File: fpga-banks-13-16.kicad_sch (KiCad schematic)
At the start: 48 parts, among them U14 XC7A100T-FGG484, U15 Oscillator_100MHz_AMJMEFB

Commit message: pcb final
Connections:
- net ROT_GPIO1: now also U14.N14 (IO_L23N_T3_A02_D18_14); no longer U14.M16 (IO_L24N_T3_RS0_15)
- net ROT_GPIO2: now also U14.U20 (IO_L11P_T1_SRCC_14); no longer U14.F21 (IO_25_16)
- net ROT_MISO: now also U14.K13 (IO_L19P_T3_A22_15); no longer U14.R19 (IO_L5N_T0_D07_14)
- net ROT_MOSI: now also U14.W20 (IO_L12N_T1_MRCC_14); no longer U14.L16 (IO_L23P_T3_FOE_B_15)
- net ROT_RDY\ROT_GPIO0: now also U14.F21 (IO_25_16); no longer U14.F20 (IO_L18N_T2_16)
- net ROT_RX: now also U14.G22 (IO_L24N_T3_16); no longer U14.N14 (IO_L23N_T3_A02_D18_14)
- net ROT_SCLK: now also U14.M16 (IO_L24N_T3_RS0_15); no longer U14.M13 (IO_L20P_T3_A20_15)
- net ROT_SS: now also U14.M13 (IO_L20P_T3_A20_15); no longer U14.U20 (IO_L11P_T1_SRCC_14)
- net ROT_TX: now also U14.F20 (IO_L18N_T2_16); no longer U14.G22 (IO_L24N_T3_16)
- net TPM_PIRQ#: now also U14.L16 (IO_L23P_T3_FOE_B_15); no longer U14.K13 (IO_L19P_T3_A22_15)
- net TPM_RST: now also U14.R19 (IO_L5N_T0_D07_14); no longer U14.W20 (IO_L12N_T1_MRCC_14)

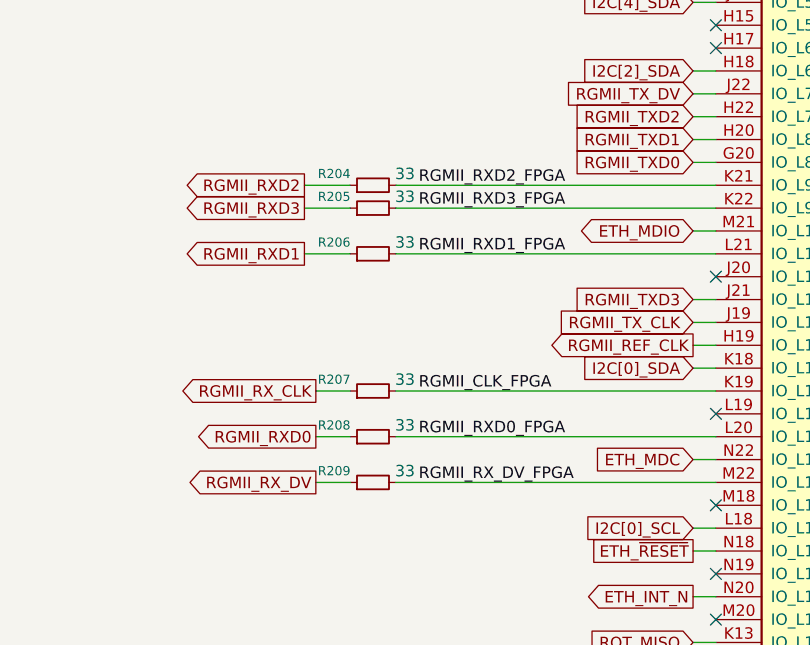
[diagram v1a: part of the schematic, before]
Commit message: bom changes
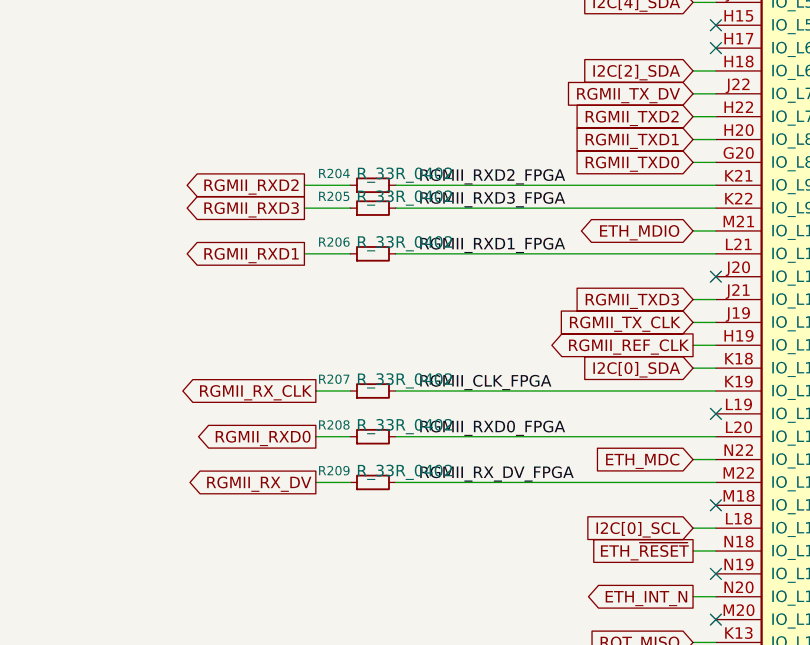
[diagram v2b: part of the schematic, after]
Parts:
- R161: MPN ERJ2GE0R00X -> RC0402JR-7D0RL; Manufacturer Panasonic -> YAGEO
- R204, R205, R206, R207, R208, R209: value 33 -> R_33R_0402

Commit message: version 1.0 complete
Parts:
- C92, C93, C94, C95: MPN C1210C476K8RACTU -> C1210C476K8RAC7210
- R133: MPN CR0402-FX-2201GLF -> AC0402FR-7D2K2L; Manufacturer Bourns -> YAGEO
- R134, R135: MPN CR0402-FX-4701GLF -> RC0402FR-7D4K7L; Manufacturer Bourns -> YAGEO
- R204, R205, R206, R207, R208, R209: MPN (none) -> MCS04020C3309FE000; Manufacturer (none) -> Vishay / Beyschlag
- U14: MPN XC7A100T-FGG484 -> XC7A100T-2FGG484C
- U15: MPN AMJMEFB-100.0000T -> ASEMB-100.000MHZ-XY-T

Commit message: "In the process of upgrading the ddr memory"
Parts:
- removed R133: R_2k2_0402, antmicro-footprints:R_0402_1005Metric, symbol antmicroResistors0402:R_2k2_0402
- removed R134, R135: R_4k7_0402, antmicro-footprints:R_0402_1005Metric, symbol antmicroResistors0402:R_4k7_0402
- removed R161: R_0R_0402, antmicro-footprints:R_0402_1005Metric, symbol antmicroResistors0402:R_0R_0402
- added R24, R25, R26, R28, R29: R_4k7_0402, Resistor_SMD:R_0402_1005Metric, symbol antmicroResistors0402:R_4k7_0402
- C92, C93, C94, C95: footprint antmicro-footprints:C_1210_3225Metric -> Capacitor_SMD:C_1210_3225Metric
- R1: footprint antmicro-footprints:R_0402_1005Metric -> Resistor_SMD:R_0402_1005Metric; now not fitted; now left out of the parts list
- R2: footprint antmicro-footprints:R_0402_1005Metric -> Resistor_SMD:R_0402_1005Metric
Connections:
- net VCC3V3: now also R24.1, R25.1, R26.1, R28.1, R29.1
- net QSPI_CS_N: now reaches U14.T19 (IO_L6P_T0_FCS_B_14)
- net QSPI_CS_N: now also R29.2
- net ESPI_ALERT_N: no longer names the net of U14.D16 (IO_L5N_T0_16)
- net ESPI_CLK: no longer names the net of U14.D17 (IO_L12P_T1_MRCC_16)
- net ESPI_CS0_N: no longer names the net of U14.E16 (IO_L5P_T0_16)
- net ESPI_CS1_N: no longer names the net of U14.H13 (IO_L1P_T0_AD0P_15)
- net ESPI_IO0: no longer names the net of U14.C14 (IO_L3P_T0_DQS_16)
- net ESPI_IO1: no longer names the net of U14.E13 (IO_L4P_T0_16)
- net ESPI_IO2: no longer names the net of U14.E17 (IO_L2N_T0_16)
- net ESPI_IO3: no longer names the net of U14.F13 (IO_L1P_T0_16)
- net ESPI_RESET_N: no longer names the net of U14.G13 (IO_L1N_T0_AD0N_15)
- net I2C[0]_SCL: no longer names the net of U14.L18 (IO_L16N_T2_A27_15)
- net I2C[0]_SDA: no longer names the net of U14.K18 (IO_L13P_T2_MRCC_15)
- net I2C[12]_SCL: no longer names the net of U14.N13 (IO_L23P_T3_A03_D19_14)
- net I2C[1]_SCL: no longer names the net of U14.K17 (IO_L21P_T3_DQS_15)
- net I2C[1]_SDA: no longer names the net of U14.K16 (IO_L23N_T3_FWE_B_15)
- net I2C[2]_SCL: no longer names the net of U14.G18 (IO_L4N_T0_15)
- net I2C[2]_SDA: no longer names the net of U14.H18 (IO_L6N_T0_VREF_15)
- net I2C[3]_SCL: no longer names the net of U14.J16 (IO_0_15)
- net I2C[3]_SDA: no longer names the net of U14.F18 (IO_L15P_T2_DQS_16)
- net I2C[4]_SCL: no longer names the net of U14.G17 (IO_L4P_T0_15)
- net I2C[4]_SDA: no longer names the net of U14.J15 (IO_L5P_T0_AD9P_15)
- net I2C[6]_SCL: no longer names the net of U14.L15 (IO_L22N_T3_A16_15)
- net I2C[6]_SDA: no longer names the net of U14.L14 (IO_L22P_T3_A17_15)
- net I2C[7]_SCL: no longer names the net of U14.G15 (IO_L2P_T0_AD8P_15)
- net I2C[7]_SDA: no longer names the net of U14.J14 (IO_L3P_T0_DQS_AD1P_15)
- net I2C[8]_SCL: no longer names the net of U14.K14 (IO_L19N_T3_A21_VREF_15)
- net I2C[8]_SDA: no longer names the net of U14.L13 (IO_L20N_T3_A19_15)
- net I2C[9]_SCL: no longer names the net of U14.P16 (IO_L24P_T3_A01_D17_14)
- net I2C[9]_SDA: no longer names the net of U14.V17 (IO_L16P_T2_CSI_B_14)
- net I3C[0]_SCL_3V3: no longer names the net of U14.C22 (IO_L20P_T3_16)
- net I3C[0]_SDA_3V3: no longer names the net of U14.F19 (IO_L18P_T2_16)
- net I3C[1]_SCL_3V3: no longer names the net of U14.B22 (IO_L20N_T3_16)
- net I3C[1]_SDA_3V3: no longer names the net of U14.C20 (IO_L19N_T3_VREF_16)
- net I3C[2]_SCL_3V3: no longer names the net of U14.A21 (IO_L21N_T3_DQS_16)
- net I3C[2]_SDA_3V3: no longer names the net of U14.B20 (IO_L16P_T2_16)
- net I3C[3]_SCL_3V3: no longer names the net of U14.A20 (IO_L16N_T2_16)
- net I3C[3]_SDA_3V3: no longer names the net of U14.A18 (IO_L17P_T2_16)
- net NCSI_CLK: no longer names the net of U14.B17 (IO_L11P_T1_SRCC_16)
- net NCSI_CRS_DV: no longer names the net of U14.A15 (IO_L9P_T1_DQS_16)
- net NCSI_RXD0: no longer names the net of U14.E14 (IO_L4N_T0_16)
- net NCSI_RXD1: no longer names the net of U14.D14 (IO_L6P_T0_16)
- net NCSI_RXER: no longer names the net of U14.A13 (IO_L10P_T1_16)
- net NCSI_TXD0: no longer names the net of U14.A14 (IO_L10N_T1_16)
- net NCSI_TXD1: no longer names the net of U14.C15 (IO_L3N_T0_DQS_16)
- net NCSI_TXEN: no longer names the net of U14.B15 (IO_L7P_T1_16)
- net PRSNT0_N_R: no longer names the net of U14.C13 (IO_L8P_T1_16)
- net ROT_GPIO1: no longer names the net of U14.N14 (IO_L23N_T3_A02_D18_14)
- net ROT_GPIO2: no longer names the net of U14.U20 (IO_L11P_T1_SRCC_14)
- net ROT_MISO: no longer names the net of U14.K13 (IO_L19P_T3_A22_15)
- net ROT_MOSI: no longer names the net of U14.W20 (IO_L12N_T1_MRCC_14)
- net ROT_QSPI_DQ0 renamed QSPI_D0
- net QSPI_D0: now also R24.2
- net ROT_QSPI_DQ1 renamed QSPI_D1
- net QSPI_D1: now also R25.2
- net ROT_QSPI_DQ2 renamed QSPI_D2
- net QSPI_D2: now also R26.2
- net ROT_QSPI_DQ3 renamed QSPI_D3
- net QSPI_D3: now also R28.2
- net ROT_RDY\ROT_GPIO0: no longer names the net of U14.F21 (IO_25_16)
- net ROT_RX: no longer names the net of U14.G22 (IO_L24N_T3_16)
- net ROT_SCLK: no longer names the net of U14.M16 (IO_L24N_T3_RS0_15)
- net ROT_SS: no longer names the net of U14.M13 (IO_L20P_T3_A20_15)
- net ROT_TX: no longer names the net of U14.F20 (IO_L18N_T2_16)
- net SGPIO_INTR_N: no longer names the net of U14.M15 (IO_L24P_T3_RS1_15)
- net SPI0_CLK_R: no longer names the net of U14.D20 (IO_L19P_T3_16)
- net SPI0_CS_N_R: no longer names the net of U14.E22 (IO_L22P_T3_16)
- net SPI0_MISO_R: no longer names the net of U14.D22 (IO_L22N_T3_16)
- net SPI0_MOSI_R: no longer names the net of U14.E21 (IO_L23P_T3_16)
- net TPM_GPIO: no longer names the net of U14.Y21 (IO_L9P_T1_DQS_14)
- net TPM_PIRQ#: no longer names the net of U14.L16 (IO_L23P_T3_FOE_B_15)
- net TPM_PP: no longer names the net of U14.M17 (IO_25_15)
- net TPM_RST: no longer names the net of U14.R19 (IO_L5N_T0_D07_14)
- net UART0_SCM_RX: no longer names the net of U14.D19 (IO_L14N_T2_SRCC_16)
- net UART0_SCM_TX: no longer names the net of U14.A19 (IO_L17N_T2_16)
- net UART1_SCM_RX: no longer names the net of U14.C19 (IO_L13N_T2_MRCC_16)
- net UART1_SCM_TX: no longer names the net of U14.A16 (IO_L9N_T1_DQS_16)
- net ULPI1_CLKOUT: no longer names the net of U14.W19 (IO_L12P_T1_MRCC_14)
- net ULPI1_DATA0: no longer names the net of U14.AB18 (IO_L17N_T2_A13_D29_14)
- net ULPI1_DATA1: no longer names the net of U14.AA18 (IO_L17P_T2_A14_D30_14)
- net ULPI1_DATA2: no longer names the net of U14.AA19 (IO_L15P_T2_DQS_RDWR_B_14)
- net ULPI1_DATA3: no longer names the net of U14.AB20 (IO_L15N_T2_DQS_DOUT_CSO_B_14)
- net ULPI1_DATA4: no longer names the net of U14.AA20 (IO_L8P_T1_D11_14)
- net ULPI1_DATA5: no longer names the net of U14.AB21 (IO_L10P_T1_D14_14)
- net ULPI1_DATA6: no longer names the net of U14.AA21 (IO_L8N_T1_D12_14)
- net ULPI1_DATA7: no longer names the net of U14.AB22 (IO_L10N_T1_D15_14)
- net ULPI1_DIR: no longer names the net of U14.W21 (IO_L7P_T1_D09_14)
- net ULPI1_NXT: no longer names the net of U14.W22 (IO_L7N_T1_D10_14)
- net ULPI1_RESET: no longer names the net of U14.V20 (IO_L11N_T1_SRCC_14)
- net ULPI1_STP: no longer names the net of U14.Y22 (IO_L9N_T1_DQS_D13_14)
- net VIRTUAL_RESEAT_R: no longer names the net of U14.B16 (IO_L7N_T1_16)
- no-connect marks 64 -> 145
